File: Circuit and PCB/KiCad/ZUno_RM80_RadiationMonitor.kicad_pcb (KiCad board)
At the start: 2 copper layers, 41.9 x 36.8 mm, 7 parts, among them U1 AdafruitSharpMemoryDisplay, U2 Z-Uno, U3 RM-60

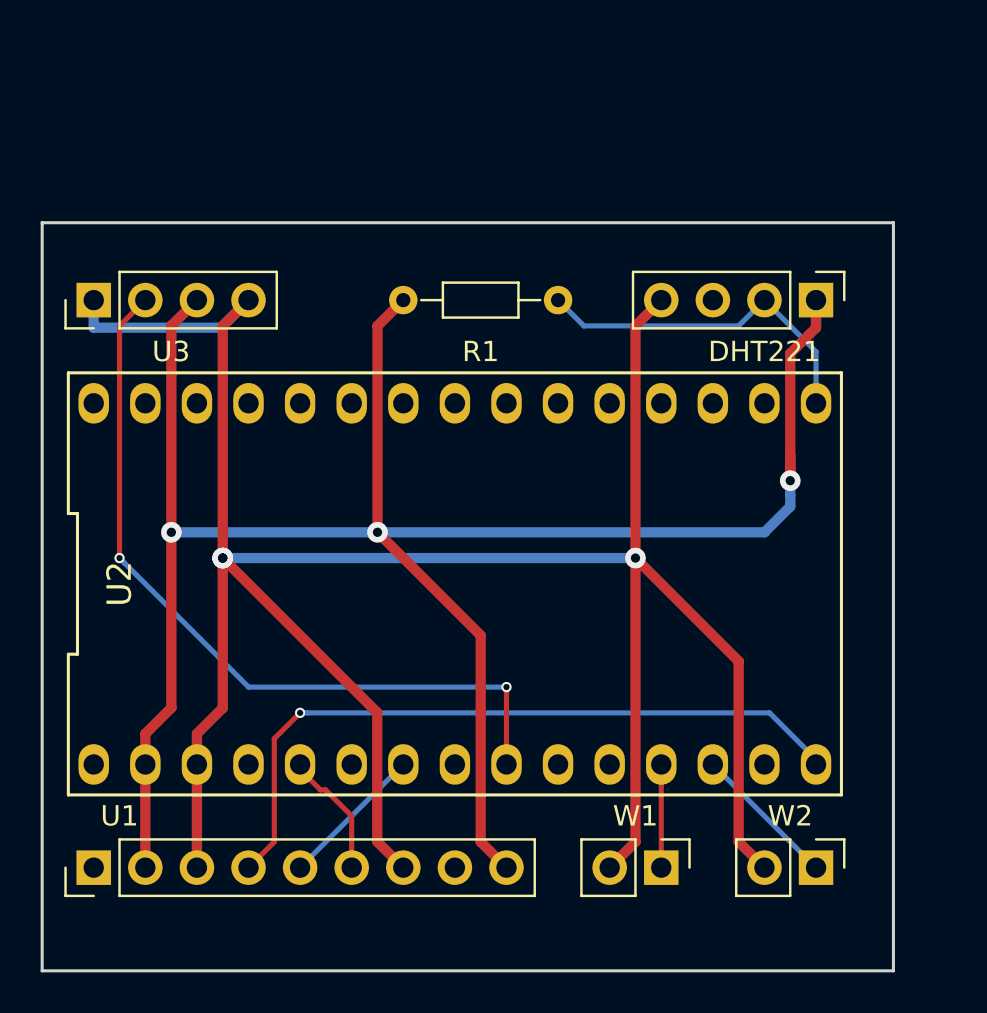
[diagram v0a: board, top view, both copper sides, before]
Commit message: Version adapted for Z-Uno firmware version 2.0.9 that supports external interrupts. The RM-80 radiation monitor has to be connected to the external interrupt 'ZUNO_EXT_ZEROX'. Only valid mean/average values are reported via Z-Wave.
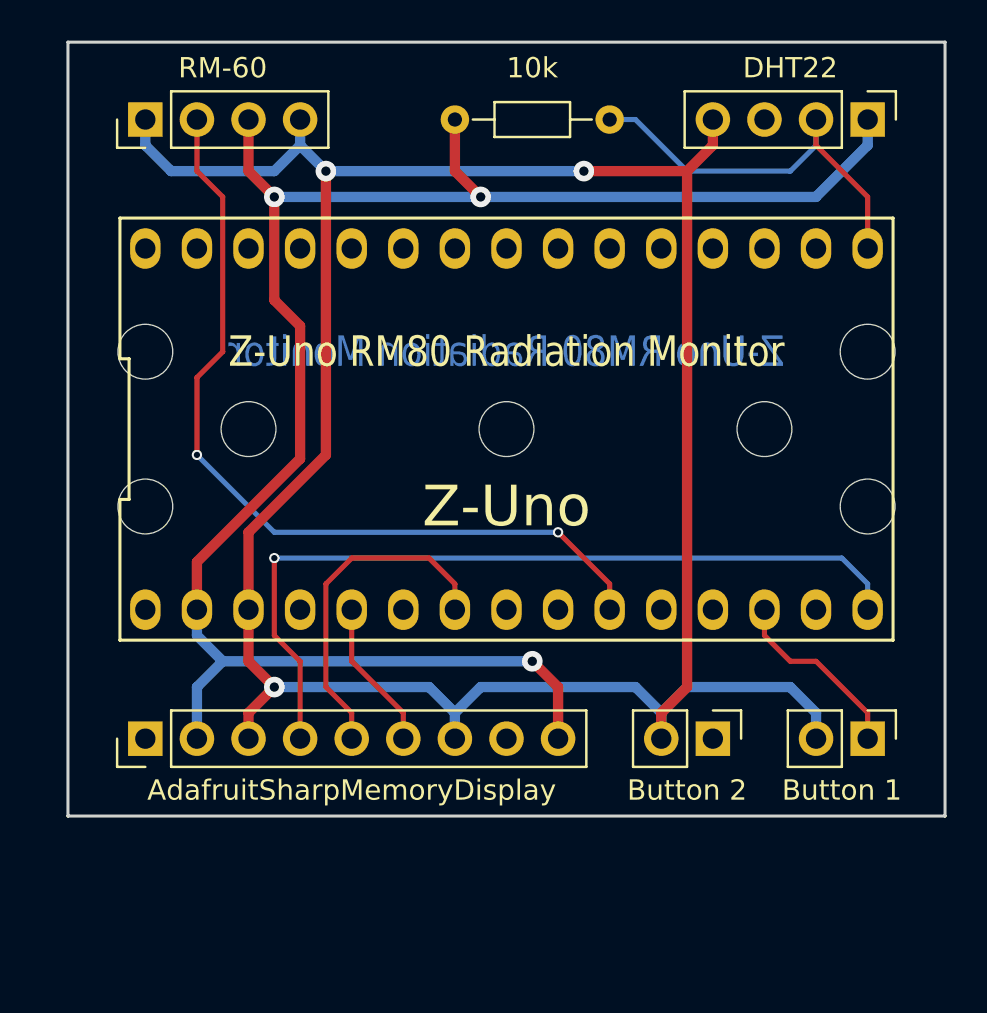
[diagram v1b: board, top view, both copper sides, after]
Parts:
- added REF**: MH_2.7mm, Mounting_Holes:MountingHole_2.7mm, F.Cu at (83.8, 41.9)
- added REF**: MH_2.7mm, Mounting_Holes:MountingHole_2.7mm, F.Cu at (83.8, 34.3)
- added REF**: MH_2.7mm, Mounting_Holes:MountingHole_2.7mm, F.Cu at (78.7, 38.1)
- added REF**: MH_2.7mm, Mounting_Holes:MountingHole_2.7mm, F.Cu at (66.0, 38.1)
- added REF**: MH_2.7mm, Mounting_Holes:MountingHole_2.7mm, F.Cu at (53.3, 38.1)
- added REF**: MH_2.7mm, Mounting_Holes:MountingHole_2.7mm, F.Cu at (48.3, 41.9)
- added REF**: MH_2.7mm, Mounting_Holes:MountingHole_2.7mm, F.Cu at (48.3, 34.3)
- R1: value R -> 10k
- moved R1 9.25 mm to (63.5, 22.9)
- moved U3 9.25 mm to (48.3, 22.9)
- moved DHT221 9.25 mm to (83.8, 22.9)
- moved U2 8.03 mm to (66.0, 38.1)
- moved W1 6.84 mm to (76.2, 53.3)
- moved U1 6.84 mm to (48.3, 53.3)
- moved W2 6.84 mm to (83.8, 53.3)
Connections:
- U2 pad 10: (no net) -> Net-(U2-Pad10)
- U2 pad 9: Net-(U2-Pad9) -> (no net)
- U3 pad 2: Net-(U2-Pad9) -> Net-(U2-Pad10)
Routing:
- net Net-(U2-Pad10): track 0.00 -> 41.8 mm, vias 0 -> 2
- net Net-(U2-Pad9): track 39.0 -> 0.00 mm, vias 2 -> 0
- net +5V: track 103.6 -> 90.1 mm
- net Net-(U1-Pad5): track 7.43 -> 16.8 mm
- net Net-(U1-Pad4): track 35.3 -> 40.4 mm
- net Net-(U2-Pad12): track 5.08 -> 0.00 mm
- net Net-(DHT221-Pad2): track 17.3 -> 20.4 mm
- net Net-(U2-Pad13): track 7.18 -> 9.20 mm
- net GND: track 124.6 -> 126.0 mm
- net Net-(U1-Pad6): track 6.53 -> 7.40 mm
- added copper zone on B.Cu, net GND
- added copper zone on F.Cu, net GND
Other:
- board size 41.9 x 36.8 mm -> 43.2 x 38.1 mm
- board text added: "Z-Uno RM80 Radiation Monitor"
